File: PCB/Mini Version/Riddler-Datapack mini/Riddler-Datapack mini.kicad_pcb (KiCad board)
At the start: 4 copper layers, 45 x 60 mm, 47 parts, among them J1 UJ20-C-H-G-SMT-1-P16-TR, J2 DISPLAY, J4 Micro_SD_Card, SW1 RST, SW2 BOOT, U1 USBLC6-2P6, U2 ESP32-S3-MINI-1, U3 TLV62568DBV

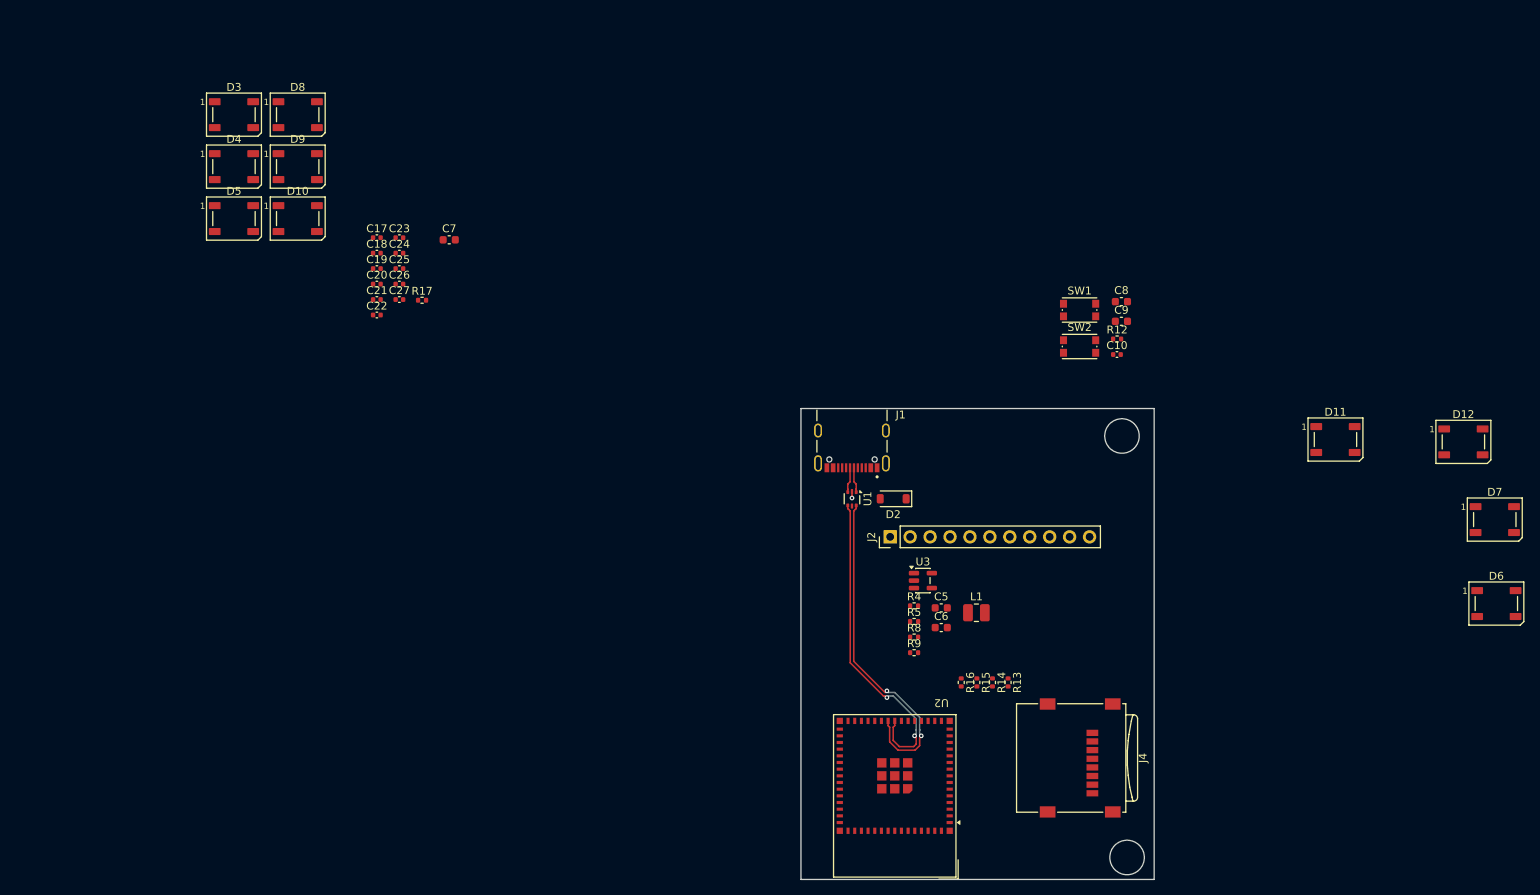
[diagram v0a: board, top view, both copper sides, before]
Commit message: feat(hardware): complete 4-layer PCB routing for Mini Datapack prop and add 3D exports
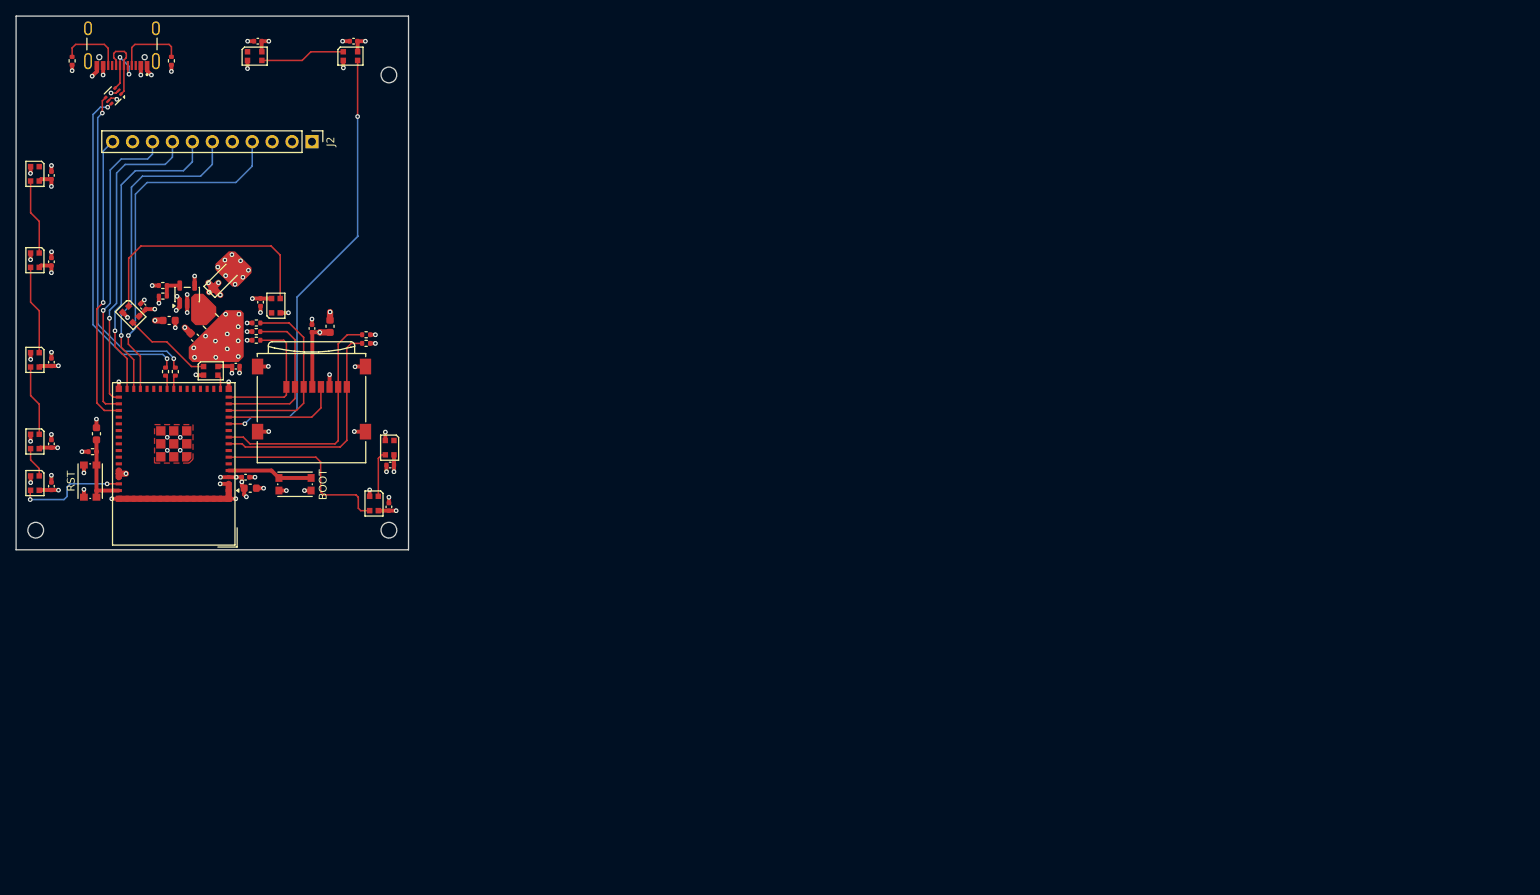
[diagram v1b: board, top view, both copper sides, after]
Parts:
- added C28: 100n, Capacitor_SMD:C_0402_1005Metric, F.Cu at (93.0, 33.2)
- added C29: 100n, Capacitor_SMD:C_0402_1005Metric, F.Cu at (80.8, 33.2)
- added D1: WS2812B-2020, LED_SMD:LED_WS2812B-2020_PLCC4_2.0x2.0mm, F.Cu at (95.6, 92.1)
- added D13: WS2812B-2020, LED_SMD:LED_WS2812B-2020_PLCC4_2.0x2.0mm, F.Cu at (80.4, 35.1)
- added R18: 22, Resistor_SMD:R_0402_1005Metric, F.Cu at (70.3, 75.3)
- added R19: 22, Resistor_SMD:R_0402_1005Metric, F.Cu at (69.0, 75.3)
- D10, D11, D12, D3, D4, D5, D6, D7, D8, D9: value WS2812B -> WS2812B-2020; footprint LED_SMD:LED_WS2812B_PLCC4_5.0x5.0mm_P3.2mm -> LED_SMD:LED_WS2812B-2020_PLCC4_2.0x2.0mm
- moved D7 186.1 mm to (52.4, 89.5), turned to -90 degrees
- moved D11 169.1 mm to (52.4, 50.1), turned to -90 degrees
- moved D6 160.1 mm to (83.1, 66.9), turned to 90 degrees
- moved D12 150.1 mm to (92.6, 35.1)
- moved C8 131.7 mm to (60.2, 83.2), turned to 90 degrees
- moved R12 131.3 mm to (59.7, 85.5)
- moved R5 128.9 mm to (57.1, 35.7), turned to -90 degrees
- moved SW1 127.9 mm to (59.4, 89.2), turned to 90 degrees
- moved R4 117.4 mm to (69.8, 35.7), turned to -90 degrees
- moved C9 113.0 mm to (79.8, 90.2)
- moved C10 112.1 mm to (79.2, 88.8)
- moved J4 108.1 mm to (87.6, 78.8), turned to 0 degrees
- moved U1 107.2 mm to (62.4, 40.2), turned to -135 degrees
- moved R9 106.5 mm to (68.7, 64.3)
- moved J1 106.2 mm to (63.5, 29.0)
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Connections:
- D10 pad 1: +3V3 -> Net-(D10-DOUT)
- D10 pad 2: Net-(D10-DOUT) -> GND
- D10 pad 3: GND -> Net-(D10-DIN)
- D10 pad 4: Net-(D10-DIN) -> +3V3
- D11 pad 1: +3V3 -> unconnected-(D11-DOUT-Pad1)
- D11 pad 2: Net-(D11-DOUT) -> GND
- D11 pad 3: GND -> Net-(D10-DOUT)
- D11 pad 4: Net-(D10-DOUT) -> +3V3
- D12 pad 1: +3V3 -> Net-(D12-DOUT)
- D12 pad 2: unconnected-(D12-DOUT-Pad2) -> GND
- D12 pad 3: GND -> /Logic/NPD_F
- D12 pad 4: Net-(D11-DOUT) -> +3V3
- D3 pad 1: +3V3 -> unconnected-(D3-DOUT-Pad1)
- D3 pad 2: Net-(D3-DOUT) -> GND
- D3 pad 3: GND -> Net-(D1-DOUT)
- D3 pad 4: /Logic/DOUT_NPM -> +3V3
- D4 pad 1: +3V3 -> Net-(D4-DOUT)
- D4 pad 2: Net-(D4-DOUT) -> GND
- D4 pad 3: GND -> /Logic/NPD_PWRS
- D4 pad 4: Net-(D3-DOUT) -> +3V3
- D5 pad 1: +3V3 -> Net-(D5-DOUT)
- D5 pad 2: Net-(D5-DOUT) -> GND
- D5 pad 3: GND -> Net-(D4-DOUT)
- D5 pad 4: Net-(D4-DOUT) -> +3V3
- D6 pad 1: +3V3 -> unconnected-(D6-DOUT-Pad1)
- D6 pad 2: Net-(D6-DOUT) -> GND
- D6 pad 3: GND -> Net-(D5-DOUT)
- D6 pad 4: Net-(D5-DOUT) -> +3V3
- D7 pad 1: +3V3 -> Net-(D7-DOUT)
- D7 pad 2: Net-(D7-DOUT) -> GND
- D7 pad 3: GND -> /Logic/NPD_LS
- D7 pad 4: Net-(D6-DOUT) -> +3V3
- D8 pad 1: +3V3 -> Net-(D8-DOUT)
- D8 pad 2: Net-(D8-DOUT) -> GND
- D8 pad 3: GND -> Net-(D7-DOUT)
- D8 pad 4: Net-(D7-DOUT) -> +3V3
- D9 pad 1: +3V3 -> Net-(D10-DIN)
- D9 pad 2: Net-(D10-DIN) -> GND
- D9 pad 3: GND -> Net-(D8-DOUT)
- D9 pad 4: Net-(D8-DOUT) -> +3V3
- U2 pad 11: /Logic/SD_MISO -> /Logic/NPD_F
- U2 pad 12: /Logic/SD_DAT1 -> /Logic/SD_CLK
- U2 pad 13: /Logic/SD_DAT2 -> /Logic/SD_MOSI
- U2 pad 14: /Logic/SD_CLK -> /Logic/CS_SD
- U2 pad 15: /Logic/SD_MOSI -> /Logic/SD_DAT2
- U2 pad 16: /Logic/CS_SD -> /Logic/NPD_PWRS
- U2 pad 23: /Logic/D- -> Net-(U2-USB_D-)
- U2 pad 24: /Logic/D+ -> Net-(U2-USB_D+)
- U2 pad 28: unconnected-(U2-IO33-Pad28) -> /Logic/SCK
- U2 pad 29: unconnected-(U2-IO34-Pad29) -> /Logic/MOSI
- U2 pad 30: unconnected-(U2-IO48-Pad30) -> /Logic/CS_TFT
- U2 pad 31: /Logic/CS_TFT -> /Logic/RST
- U2 pad 32: /Logic/RST -> /Logic/DC
- U2 pad 33: /Logic/DC -> /Logic/PWM_TFT
- U2 pad 34: /Logic/SCK -> unconnected-(U2-IO38-Pad34)
- U2 pad 35: /Logic/MOSI -> unconnected-(U2-IO39-Pad35)
- U2 pad 36: /Logic/PWM_TFT -> unconnected-(U2-IO40-Pad36)
- U2 pad 44: unconnected-(U2-IO46-Pad44) -> /Logic/NPD_LS
- U2 pad 6: unconnected-(U2-IO2-Pad6) -> /Logic/NPD_RS
- U2 pad 8: unconnected-(U2-IO4-Pad8) -> /Logic/SD_DAT1
- U2 pad 9: /Logic/DOUT_NPM -> /Logic/SD_MISO
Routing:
- net GND: track 0.83 -> 69.6 mm, vias 1 -> 58
- net /Logic/NPD_F: track 0.00 -> 57.2 mm, vias 0 -> 2
- net +3V3: track 0.00 -> 49.0 mm, vias 0 -> 36
- net /Logic/SCK: track 0.00 -> 45.3 mm, vias 0 -> 1
- net /Logic/MOSI: track 0.00 -> 41.3 mm, vias 0 -> 1
- net /Logic/CS_TFT: track 0.00 -> 39.8 mm, vias 0 -> 1
- net /Logic/RST: track 0.00 -> 39.8 mm, vias 0 -> 1
- net /Logic/DC: track 0.00 -> 39.8 mm, vias 0 -> 1
- net /Logic/PWM_TFT: track 0.00 -> 37.3 mm, vias 0 -> 1
- net Net-(D5-DOUT): track 0.00 -> 32.1 mm
- net /Logic/SD_MISO: track 0.00 -> 30.3 mm
- net /Logic/SD_DAT1: track 0.00 -> 29.5 mm
- net /Logic/SD_MOSI: track 0.00 -> 24.6 mm
- net /Logic/NPD_RS: track 0.00 -> 23.8 mm
- net /Logic/CS_SD: track 0.00 -> 21.0 mm
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- added copper zone on In2.Cu, net +3V3
- added copper zone on F.Cu, net GND
- added copper zone on In1.Cu, net GND
- added copper zone on In2.Cu, net Net-(D2-K)
- added copper zone on In2.Cu, net VBUS
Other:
- board size 45 x 60 mm -> 50 x 68 mm

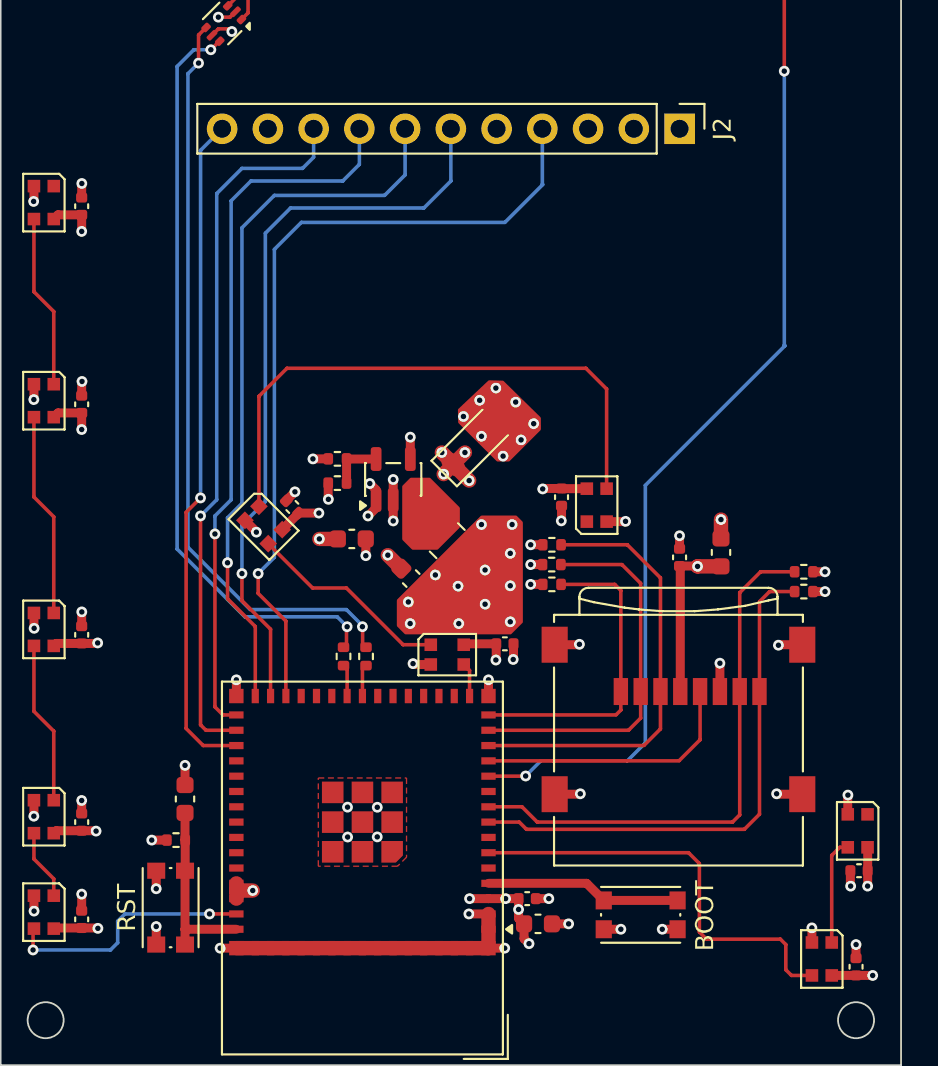
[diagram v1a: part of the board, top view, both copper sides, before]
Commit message: Minor updates including: silkscreen design, and changed out the button
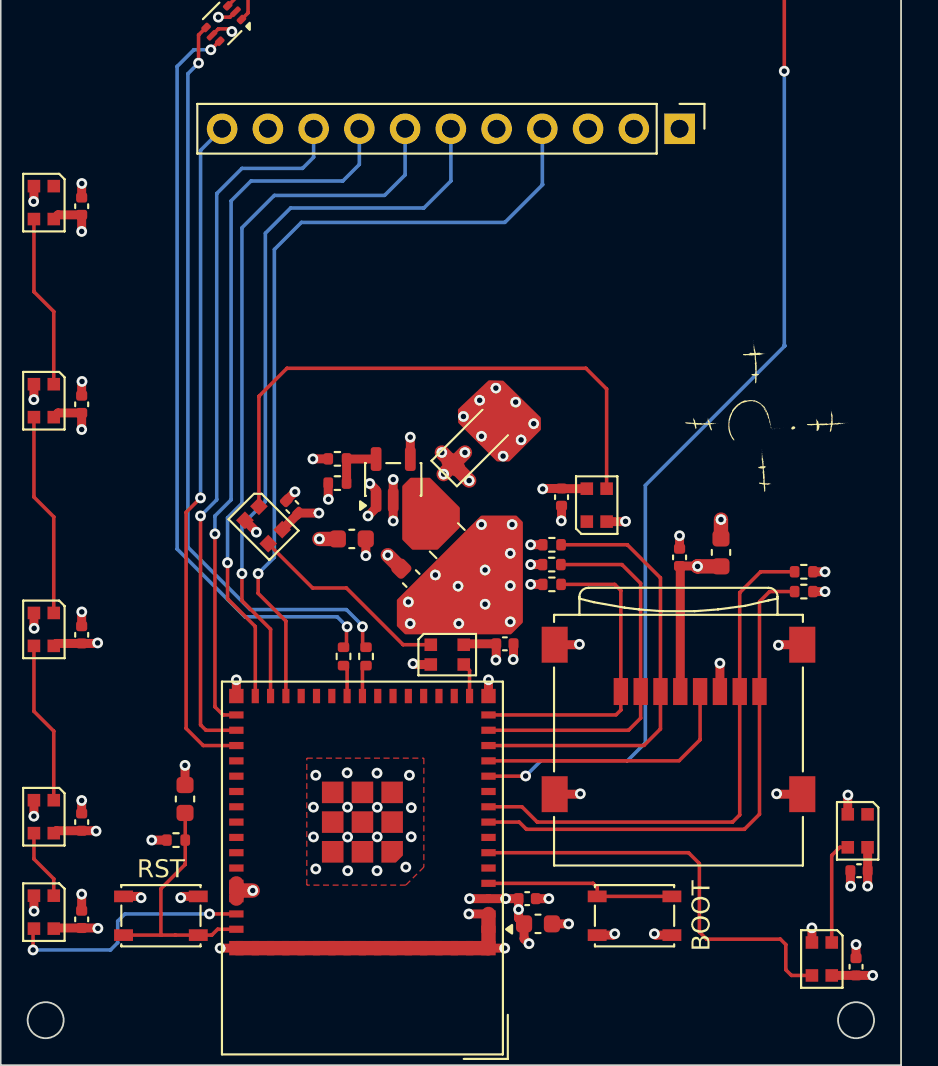
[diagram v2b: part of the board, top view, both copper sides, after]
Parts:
- added G***: LOGO, Symbol footprints:Riddler-zodiac-2, F.Cu at (92.9, 61.6)
- added G***: LOGO, Symbol footprints:Riddler-questionmark, B.Cu at (86.5, 68.0)
- added G***: LOGO, Symbol footprints:Riddler-questionmark, B.Cu at (62.0, 64.7)
- added G***: LOGO, Symbol footprints:Riddler-questionmark, B.Cu at (74.9, 58.8)
- SW1, SW2: footprint Button_Switch_SMD:SW_Push_1P1T_NO_CK_KMR2 -> Button_Switch_SMD:SW_SPST_PTS810
- moved SW1 0.70 mm to (58.9, 89.7), turned to 0 degrees
- moved SW2 0.34 mm to (85.2, 89.7)
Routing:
- net /Logic/EN: track 10.2 -> 13.7 mm
- net GND: track 69.6 -> 69.8 mm, vias 58 -> 70
